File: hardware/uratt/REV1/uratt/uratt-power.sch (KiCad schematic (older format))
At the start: 68 parts, among them J6 Conn_01x02, J7 Conn_01x02, J8 Conn_01x02, SW4 SW_SPDT, U4 MCP73832T-2ACI/OT, U5 TPS2115APWR, U6 TPS61032PWP, U7 AP2112K-3.3TRG1, U8 AP2112K-3.3TRG1, U9 MP6513GJ-Z

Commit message: work in progress on REV1 schematic/PCB
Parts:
- added C35: 100uF, Capacitor_SMD:CP_Elec_5x3, symbol Device:CP1_Small
- added Q5: 2N7002, Package_TO_SOT_SMD:SOT-23, symbol Transistor_FET:2N7002
- added Q6: DMP31D0U, Package_TO_SOT_SMD:SOT-23, symbol Transistor_FET:BSS83P
- added R32, R60: 1K, Resistor_SMD:R_0603_1608Metric, symbol Device:R_Small_US
- added R33: 10K, Resistor_SMD:R_0603_1608Metric, symbol Device:R_Small_US
- added TP8: TestPoint, TestPoint:TestPoint_Pad_D1.0mm, symbol Connector:TestPoint
- renumbered R32 to 3M1, R33 to 510K1
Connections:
- net +VSW: now also U6.8 (SYNC), C35.1, Q6.2 (S), R33.2
- net GND: now also J7.2 (Pin_2), C35.2, Q5.2 (S), TP8.1; no longer J7.1 (Pin_1), U6.8 (SYNC)
- net PWR_ENABLE: now also R32.2; no longer R34.2, U6.9 (EN)
- net at SW4.2 (B): now also J7.1 (Pin_1); no longer J7.2 (Pin_2)
- new net: Q5.1 (G), R32.1
- new net: Q5.3 (D), R33.1, R60.2
- new net: Q6.1 (G), R60.1
- new net: Q6.3 (D), R34.2, U6.9 (EN)
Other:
- moved on the sheet: 3M1, 510K1, C23, C24, C27, C28, C29, D10, D11, GT1, J7, L1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

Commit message: uratt REV1 work, remove front panel, place new parts, partial routing
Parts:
- L1: footprint Inductor_SMD:L_12x12mm_H4.5mm -> Inductor_SMD:L_6.3x6.3_H3
- renumbered C35 to C21, C21 to C22, C22 to C23, C25 to C24, C26 to C25, C23 to C26, C24 to C27, C27 to C28, C28 to C29, C29 to C30, C30 to C31, C31 to C32, D9 to D10, D10 to D11, D11 to D12, D12 to D7, D7 to D8, D8 to D9, Q5 to Q3, Q6 to Q4, R26 to R31, R27 to R32, R28 to R33, R29 to R34, R30 to R35, R31 to R36, R32 to R37, R35 to R38, R33 to R39, R36 to R40, R60 to R41, R34 to R42, R37 to R43, R38 to R44, 3M1 to R45, 510K1 to R46, R39 to R47, R40 to R48, R41 to R49, R42 to R50, SW4 to SW3, TP7 to TP6, TP8 to TP7, TP6 to TP8, U7 to U6, U8 to U7, U6 to U8

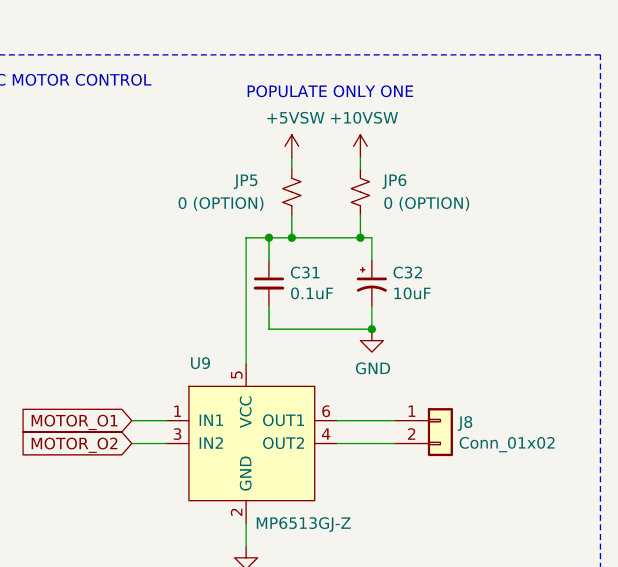
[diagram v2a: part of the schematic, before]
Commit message: uRATT REV1 progress.  placed and mostly routed.
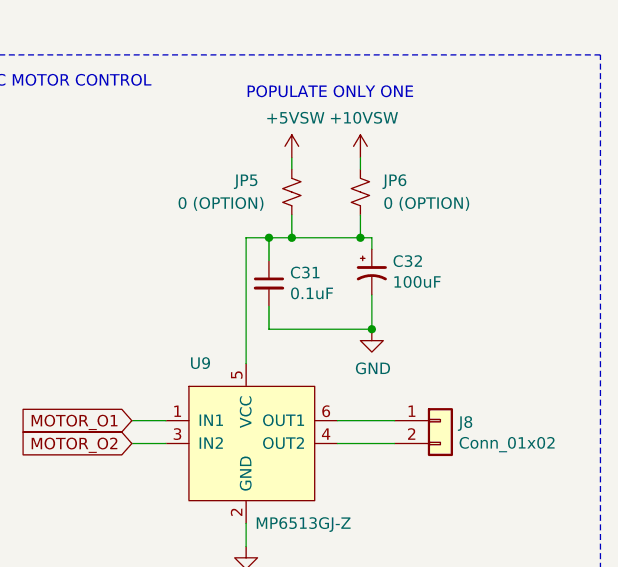
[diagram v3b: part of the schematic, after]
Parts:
- C32: value 10uF -> 100uF; footprint Capacitor_SMD:C_0805_2012Metric -> Capacitor_SMD:CP_Elec_5x3; Digikey 1276-1096-1-ND -> PCE4156CT-ND
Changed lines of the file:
@@
 Connection ~ 2350 8250
-$Comp
-L Device:CP1_Small C?
-U 1 1 63772D7F
-P 14600 6300
-AR Path="/63772D7F" Ref="C?"  Part="1"
-AR Path="/61FC99B5/63772D7F" Ref="C32"  Part="1"
-F 0 "C32" H 14691 6346 50  0000 L CNN
-F 1 "10uF" H 14691 6255 50  0000 L CNN
-F 2 "Capacitor_SMD:C_0805_2012Metric" H 14600 6300 50  0001 C CNN
-F 3 "http://www.samsungsem.com/kr/support/product-search/mlcc/CL21A106KOQNNNE.jsp" H 14600 6300 50  0001 C CNN
-F 4 "1276-1096-1-ND" H 14600 6300 50  0001 C CNN "Digikey"
-	1    14600 6300
-	1    0    0    -1
-$EndComp
 $Comp
 L Device:C_Small C?
@@
 	14150 6500 14600 6500
 Wire Wire Line
-	14600 6500 14600 6400
-Wire Wire Line
-	14600 6100 14600 6200
-Wire Wire Line
 	14150 6200 14150 6100
 Connection ~ 14150 6100
@@
 	1    0    0    -1
 $EndComp
-Connection ~ 14600 6500
 $Comp
 L Connector_Generic:Conn_01x02 J?
@@
 Wire Wire Line
 	4350 4450 4350 4400
+$Comp
+L Device:CP1_Small C?
+U 1 1 60170402
+P 14600 6250
+AR Path="/60170402" Ref="C?"  Part="1"
+AR Path="/61FC99B5/60170402" Ref="C32"  Part="1"
+F 0 "C32" H 14691 6296 50  0000 L CNN
+F 1 "100uF" H 14691 6205 50  0000 L CNN
+F 2 "Capacitor_SMD:CP_Elec_5x3" H 14600 6250 50  0001 C CNN
+F 3 "https://industrial.panasonic.com/cdbs/www-data/pdf/RDE0000/ABA0000C1151.pdf" H 14600 6250 50  0001 C CNN
+F 4 "PCE4156CT-ND" H 14600 6250 50  0001 C CNN "Digikey"
+	1    14600 6250
+	1    0    0    -1
+$EndComp
+Connection ~ 14600 6500
+Wire Wire Line
+	14600 6500 14600 6350
+Wire Wire Line
+	14600 6100 14600 6150
 $EndSCHEMATC

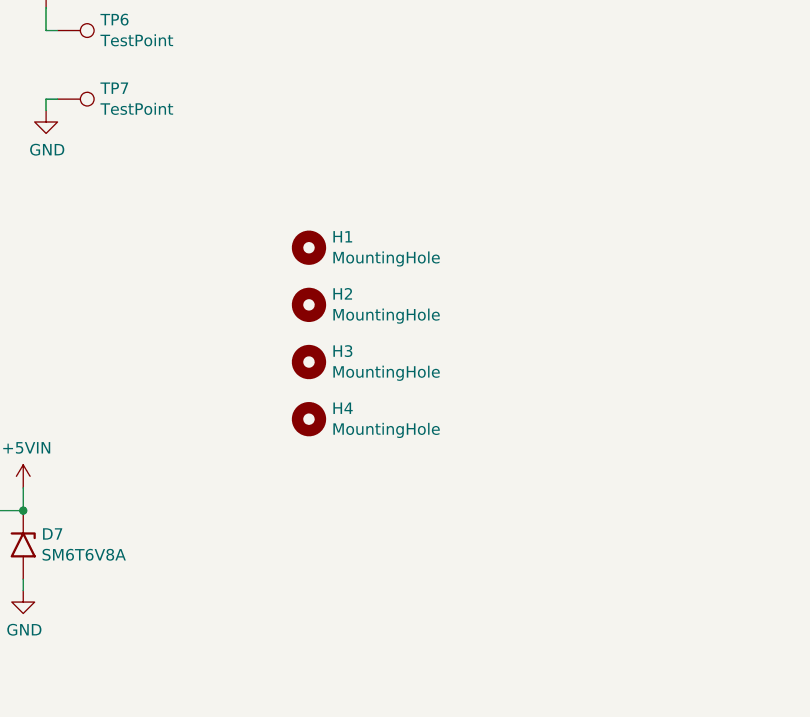
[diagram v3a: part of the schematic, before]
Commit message: complete relayout of 5V boost switcher, add plated mount holes w/FB GND ties, passes DRC
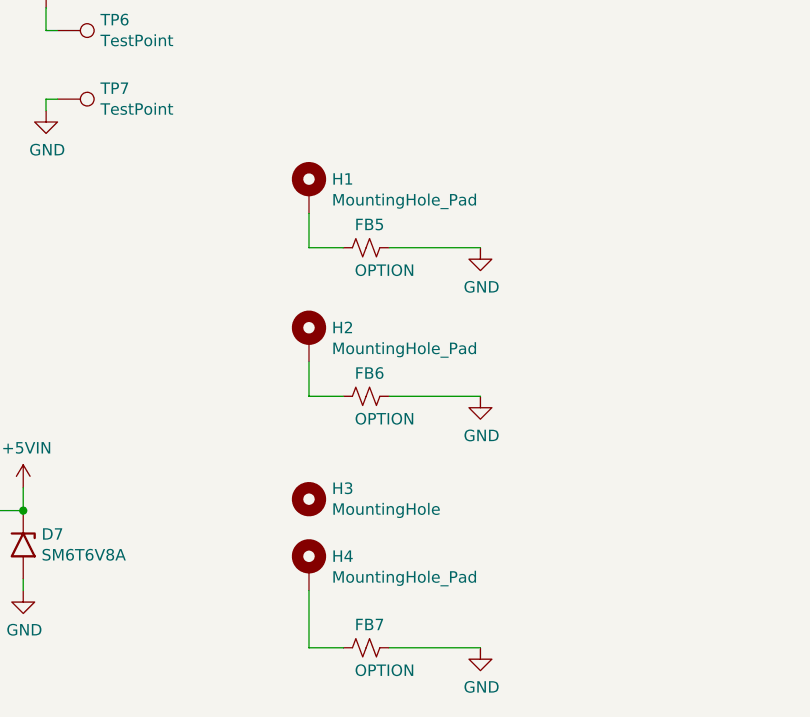
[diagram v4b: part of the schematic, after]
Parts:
- removed H1, H2, H4: MountingHole, MountingHole:MountingHole_2.7mm_M2.5, symbol Mechanical:MountingHole
- added FB5, FB6, FB7: OPTION, Resistor_SMD:R_0603_1608Metric, symbol Device:R_Small_US
- added H1, H2, H4: MountingHole_Pad, MountingHole:MountingHole_2.7mm_M2.5_Pad_TopBottom, symbol Mechanical:MountingHole_Pad
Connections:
- net GND: now also FB5.1, FB6.1, FB7.1
- new net: FB7.2, H4.1
- new net: FB5.2, H1.1
- new net: FB6.2, H2.1
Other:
- moved on the sheet: H3
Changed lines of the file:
@@
 MOTOR_O2
-$Comp
-L Mechanical:MountingHole H1
-U 1 1 5FE95DC9
-P 4350 8300
-F 0 "H1" H 4450 8346 50  0000 L CNN
-F 1 "MountingHole" H 4450 8255 50  0000 L CNN
-F 2 "MountingHole:MountingHole_2.7mm_M2.5" H 4350 8300 50  0001 C CNN
-F 3 "" H 4350 8300 50  0001 C CNN
-F 4 "" H 4350 8300 50  0001 C CNN "Field4"
-F 5 "N/A" H 4350 8300 50  0001 C CNN "Digikey"
-	1    4350 8300
-	1    0    0    -1
-$EndComp
-$Comp
-L Mechanical:MountingHole H2
-U 1 1 5FE9623B
-P 4350 8550
-F 0 "H2" H 4450 8596 50  0000 L CNN
-F 1 "MountingHole" H 4450 8505 50  0000 L CNN
-F 2 "MountingHole:MountingHole_2.7mm_M2.5" H 4350 8550 50  0001 C CNN
-F 3 "" H 4350 8550 50  0001 C CNN
-F 4 "" H 4350 8550 50  0001 C CNN "Field4"
-F 5 "N/A" H 4350 8550 50  0001 C CNN "Digikey"
-	1    4350 8550
-	1    0    0    -1
-$EndComp
 $Comp
 L Mechanical:MountingHole H3
 U 1 1 5FEA2774
-P 4350 8800
-F 0 "H3" H 4450 8846 50  0000 L CNN
-F 1 "MountingHole" H 4450 8755 50  0000 L CNN
-F 2 "MountingHole:MountingHole_2.7mm_M2.5" H 4350 8800 50  0001 C CNN
-F 3 "" H 4350 8800 50  0001 C CNN
-F 4 "" H 4350 8800 50  0001 C CNN "Field4"
-F 5 "N/A" H 4350 8800 50  0001 C CNN "Digikey"
-	1    4350 8800
-	1    0    0    -1
-$EndComp
-$Comp
-L Mechanical:MountingHole H4
-U 1 1 5FEAED48
-P 4350 9050
-F 0 "H4" H 4450 9096 50  0000 L CNN
-F 1 "MountingHole" H 4450 9005 50  0000 L CNN
-F 2 "MountingHole:MountingHole_2.7mm_M2.5" H 4350 9050 50  0001 C CNN
-F 3 "" H 4350 9050 50  0001 C CNN
-F 4 "" H 4350 9050 50  0001 C CNN "Field4"
-F 5 "N/A" H 4350 9050 50  0001 C CNN "Digikey"
-	1    4350 9050
+P 4350 9400
+F 0 "H3" H 4450 9446 50  0000 L CNN
+F 1 "MountingHole" H 4450 9355 50  0000 L CNN
+F 2 "MountingHole:MountingHole_2.7mm_M2.5" H 4350 9400 50  0001 C CNN
+F 3 "" H 4350 9400 50  0001 C CNN
+F 4 "" H 4350 9400 50  0001 C CNN "Field4"
+F 5 "N/A" H 4350 9400 50  0001 C CNN "Digikey"
+	1    4350 9400
 	1    0    0    -1
 $EndComp
@@
 Wire Wire Line
 	14600 6100 14600 6150
+$Comp
+L Mechanical:MountingHole_Pad H4
+U 1 1 6015897E
+P 4350 9700
+F 0 "H4" H 4450 9749 50  0000 L CNN
+F 1 "MountingHole_Pad" H 4450 9658 50  0000 L CNN
+F 2 "MountingHole:MountingHole_2.7mm_M2.5_Pad_TopBottom" H 4350 9700 50  0001 C CNN
+F 3 "~" H 4350 9700 50  0001 C CNN
+	1    4350 9700
+	1    0    0    -1
+$EndComp
+$Comp
+L Device:R_Small_US JP?
+U 1 1 6016F155
+P 4600 10050
+AR Path="/6016F155" Ref="JP?"  Part="1"
+AR Path="/61FC99B5/6016F155" Ref="FB7"  Part="1"
+F 0 "FB7" V 4500 10000 50  0000 L CNN
+F 1 "OPTION" V 4700 10000 50  0000 L CNN
+F 2 "Resistor_SMD:R_0603_1608Metric" H 4600 10050 50  0001 C CNN
+F 3 "~" H 4600 10050 50  0001 C CNN
+F 4 "2019-RK73Z1JTTDCT-ND" H 4600 10050 50  0001 C CNN "Digikey"
+	1    4600 10050
+	0    1    1    0
+$EndComp
+$Comp
+L power:GND #PWR?
+U 1 1 601800AD
+P 5100 10050
+AR Path="/601800AD" Ref="#PWR?"  Part="1"
+AR Path="/61FC99B5/601800AD" Ref="#PWR0103"  Part="1"
+F 0 "#PWR0103" H 5100 9800 50  0001 C CNN
+F 1 "GND" H 5105 9877 50  0000 C CNN
+F 2 "" H 5100 10050 50  0001 C CNN
+F 3 "" H 5100 10050 50  0001 C CNN
+	1    5100 10050
+	1    0    0    -1
+$EndComp
+Wire Wire Line
+	4350 9800 4350 10050
+Wire Wire Line
+	4350 10050 4500 10050
+Wire Wire Line
+	4700 10050 5100 10050
+$Comp
+L Mechanical:MountingHole_Pad H1
+U 1 1 601B9F9A
+P 4350 8050
+F 0 "H1" H 4450 8099 50  0000 L CNN
+F 1 "MountingHole_Pad" H 4450 8008 50  0000 L CNN
+F 2 "MountingHole:MountingHole_2.7mm_M2.5_Pad_TopBottom" H 4350 8050 50  0001 C CNN
+F 3 "~" H 4350 8050 50  0001 C CNN
+	1    4350 8050
+	1    0    0    -1
+$EndComp
+$Comp
+L Mechanical:MountingHole_Pad H2
+U 1 1 601C9D7C
+P 4350 8700
+F 0 "H2" H 4450 8749 50  0000 L CNN
+F 1 "MountingHole_Pad" H 4450 8658 50  0000 L CNN
+F 2 "MountingHole:MountingHole_2.7mm_M2.5_Pad_TopBottom" H 4350 8700 50  0001 C CNN
+F 3 "~" H 4350 8700 50  0001 C CNN
+	1    4350 8700
+	1    0    0    -1
+$EndComp
+$Comp
+L Device:R_Small_US FB?
+U 1 1 601F19BA
+P 4600 8300
+AR Path="/601F19BA" Ref="FB?"  Part="1"
+AR Path="/61FC99B5/601F19BA" Ref="FB5"  Part="1"
+F 0 "FB5" V 4500 8250 50  0000 L CNN
+F 1 "OPTION" V 4700 8250 50  0000 L CNN
+F 2 "Resistor_SMD:R_0603_1608Metric" H 4600 8300 50  0001 C CNN
+F 3 "~" H 4600 8300 50  0001 C CNN
+F 4 "2019-RK73Z1JTTDCT-ND" H 4600 8300 50  0001 C CNN "Digikey"
+	1    4600 8300
+	0    1    1    0
+$EndComp
+$Comp
+L power:GND #PWR?
+U 1 1 601F19C0
+P 5100 8300
+AR Path="/601F19C0" Ref="#PWR?"  Part="1"
+AR Path="/61FC99B5/601F19C0" Ref="#PWR0104"  Part="1"
+F 0 "#PWR0104" H 5100 8050 50  0001 C CNN
+F 1 "GND" H 5105 8127 50  0000 C CNN
+F 2 "" H 5100 8300 50  0001 C CNN
+F 3 "" H 5100 8300 50  0001 C CNN
+	1    5100 8300
+	1    0    0    -1
+$EndComp
+Wire Wire Line
+	4350 8300 4500 8300
+Wire Wire Line
+	4700 8300 5100 8300
+$Comp
+L Device:R_Small_US FB?
+U 1 1 6020219E
+P 4600 8950
+AR Path="/6020219E" Ref="FB?"  Part="1"
+AR Path="/61FC99B5/6020219E" Ref="FB6"  Part="1"
+F 0 "FB6" V 4500 8900 50  0000 L CNN
+F 1 "OPTION" V 4700 8900 50  0000 L CNN
+F 2 "Resistor_SMD:R_0603_1608Metric" H 4600 8950 50  0001 C CNN
+F 3 "~" H 4600 8950 50  0001 C CNN
+F 4 "2019-RK73Z1JTTDCT-ND" H 4600 8950 50  0001 C CNN "Digikey"
+	1    4600 8950
+	0    1    1    0
+$EndComp
+$Comp
+L power:GND #PWR?
+U 1 1 602021A4
+P 5100 8950
+AR Path="/602021A4" Ref="#PWR?"  Part="1"
+AR Path="/61FC99B5/602021A4" Ref="#PWR0105"  Part="1"
+F 0 "#PWR0105" H 5100 8700 50  0001 C CNN
+F 1 "GND" H 5105 8777 50  0000 C CNN
+F 2 "" H 5100 8950 50  0001 C CNN
+F 3 "" H 5100 8950 50  0001 C CNN
+	1    5100 8950
+	1    0    0    -1
+$EndComp
+Wire Wire Line
+	4350 8950 4500 8950
+Wire Wire Line
+	4700 8950 5100 8950
+Wire Wire Line
+	4350 8800 4350 8950
+Wire Wire Line
+	4350 8150 4350 8300
 $EndSCHEMATC

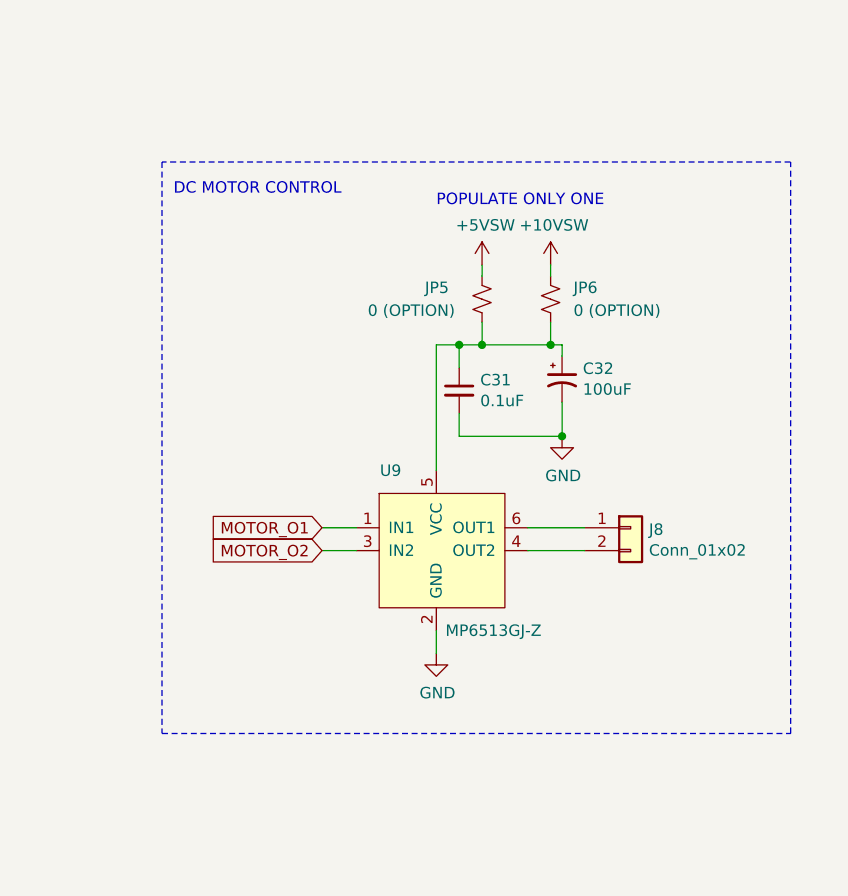
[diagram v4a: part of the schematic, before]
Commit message: uratt REV1 change inductor, cleanups, add 3.3V motor option, silk work, 12 pin FFC
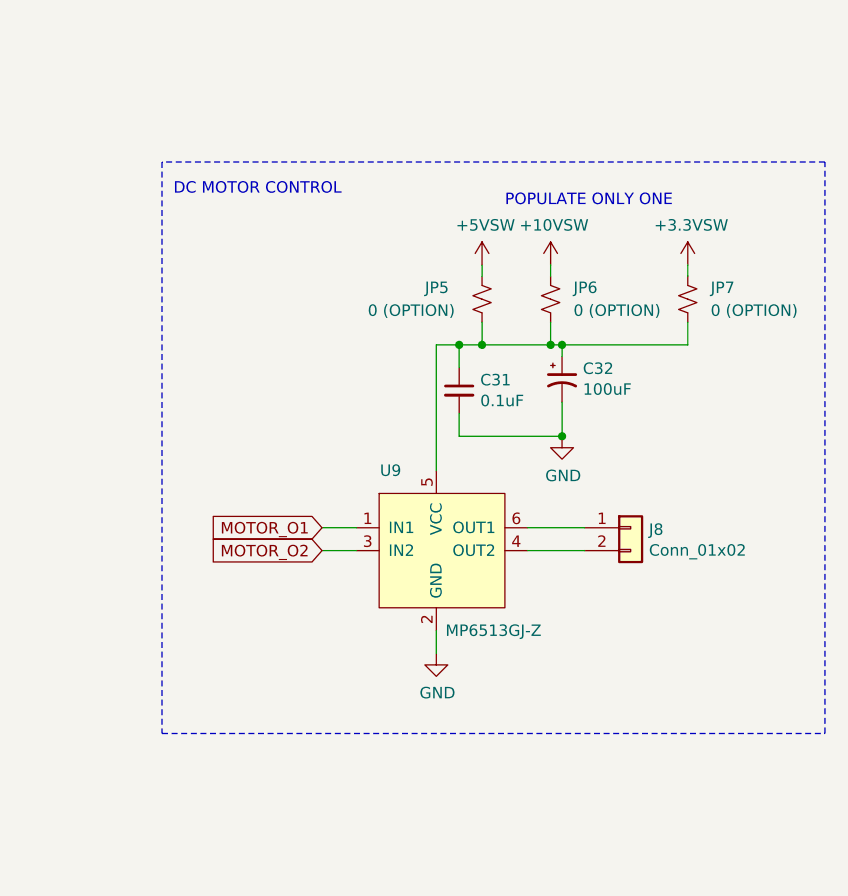
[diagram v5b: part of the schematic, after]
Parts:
- added JP7: 0 (OPTION), Resistor_SMD:R_0603_1608Metric, symbol Device:R_Small_US
- L1: footprint Inductor_SMD:L_6.3x6.3_H3 -> uratt:SRR6603-6R8ML
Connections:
- net +3.3VSW: now also JP7.1
- net at C31.1, C32.1, JP5.2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: now also JP7.2
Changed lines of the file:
@@
 F 0 "L1" H 9050 2150 50  0000 L CNN
 F 1 "6.8uH" H 9050 2050 50  0000 L CNN
-F 2 "Inductor_SMD:L_6.3x6.3_H3" H 9000 2050 50  0001 C CNN
+F 2 "uratt:SRR6603-6R8ML" H 9000 2050 50  0001 C CNN
 F 3 "http://products.sumida.com/products/pdf/CDRH124.pdf" H 9000 2050 50  0001 C CNN
 F 4 "" H 8950 2450 50  0000 C CNN "Field4"
@@
 	12850 5300 12850 7800
 Wire Notes Line
-	12850 7800 15600 7800
+	12850 7800 15750 7800
 Wire Notes Line
-	15600 7800 15600 5300
+	15750 7800 15750 5300
 Wire Notes Line
-	15600 5300 12850 5300
+	15750 5300 12850 5300
 Text Notes 12900 5450 0    50   ~ 0
 DC MOTOR CONTROL
@@
 Wire Wire Line
 	14550 6100 14600 6100
-Text Notes 14050 5500 0    50   ~ 0
+Text Notes 14350 5500 0    50   ~ 0
 POPULATE ONLY ONE
 Wire Notes Line
@@
 Wire Wire Line
 	4350 8150 4350 8300
+$Comp
+L Device:R_Small_US JP?
+U 1 1 6006C2AB
+P 15150 5900
+AR Path="/6006C2AB" Ref="JP?"  Part="1"
+AR Path="/61FC99B5/6006C2AB" Ref="JP7"  Part="1"
+F 0 "JP7" H 15250 5950 50  0000 L CNN
+F 1 "0 (OPTION)" H 15250 5850 50  0000 L CNN
+F 2 "Resistor_SMD:R_0603_1608Metric" H 15150 5900 50  0001 C CNN
+F 3 "~" H 15150 5900 50  0001 C CNN
+F 4 "2019-RK73Z1JTTDCT-ND" H 15150 5900 50  0001 C CNN "Digikey"
+	1    15150 5900
+	1    0    0    -1
+$EndComp
+Wire Wire Line
+	15150 5750 15150 5800
+Wire Wire Line
+	15150 6000 15150 6100
+Wire Wire Line
+	15150 6100 14600 6100
+Connection ~ 14600 6100
+$Comp
+L uratt:+3.3VSW #PWR?
+U 1 1 600C9279
+P 15150 5750
+AR Path="/600C9279" Ref="#PWR?"  Part="1"
+AR Path="/61FC99B5/600C9279" Ref="#PWR0106"  Part="1"
+F 0 "#PWR0106" H 15150 5600 50  0001 C CNN
+F 1 "+3.3VSW" H 15165 5923 50  0000 C CNN
+F 2 "" H 15150 5750 50  0001 C CNN
+F 3 "" H 15150 5750 50  0001 C CNN
+	1    15150 5750
+	1    0    0    -1
+$EndComp
 $EndSCHEMATC
